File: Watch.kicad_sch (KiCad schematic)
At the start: 47 parts, among them J1 USB_C_Receptacle_USB2.0_14P, Q1 2N3904, Q2 2N3904, Q3 2N3904, Q4 2N3904, SW1 SW_Push, SW3 SW_Push, SW4 SW_Push, U1 MCP73831-2-OT, U2 KCSA02-105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

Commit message: session 2
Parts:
- removed C3: C, Capacitor_SMD:C_0603_1608Metric, symbol Device:C
- removed R13, R14, R15, R16: 150, Resistor_SMD:R_0603_1608Metric, symbol Device:R
- C2, C4: value C -> 4.7µF
- R10, R11, R12, R5: footprint Resistor_SMD:R_0603_1608Metric -> (none)
- renumbered U2 to Dig1, U4 to Dig2, U5 to Dig3, U6 to Dig4
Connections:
- net A: now also U7.5 (PA04); no longer R5.1
- net B: now also U7.6 (PA05); no longer R10.1
- net C: now also U7.7 (PA06); no longer R11.1
- net D: now also U7.8 (PA07); no longer R12.1
- net DIG1: now also R5.1; no longer Dig1.3 (CA), Dig1.8 (CA)
- net DIG2: now also R10.1; no longer Dig2.3 (CA), Dig2.8 (CA)
- net DIG3: now also R11.1; no longer Dig3.3 (CA), Dig3.8 (CA)
- net DIG4: now also R12.1; no longer Dig4.3 (CA), Dig4.8 (CA)
- net DP: now also U7.14 (PA11)
- net E: now also U7.11 (PA08)
- net F: now also U7.12 (PA09)
- net G: now also U7.13 (PA10)
- net at R5.2: now also Dig1.3 (CA), Dig1.8 (CA); no longer U7.5 (PA04)
- net at R10.2: now also Dig2.3 (CA), Dig2.8 (CA); no longer U7.6 (PA05)
- net at R11.2: now also Dig3.3 (CA), Dig3.8 (CA); no longer U7.7 (PA06)
- net at R12.2: now also Dig4.3 (CA), Dig4.8 (CA); no longer U7.8 (PA07)

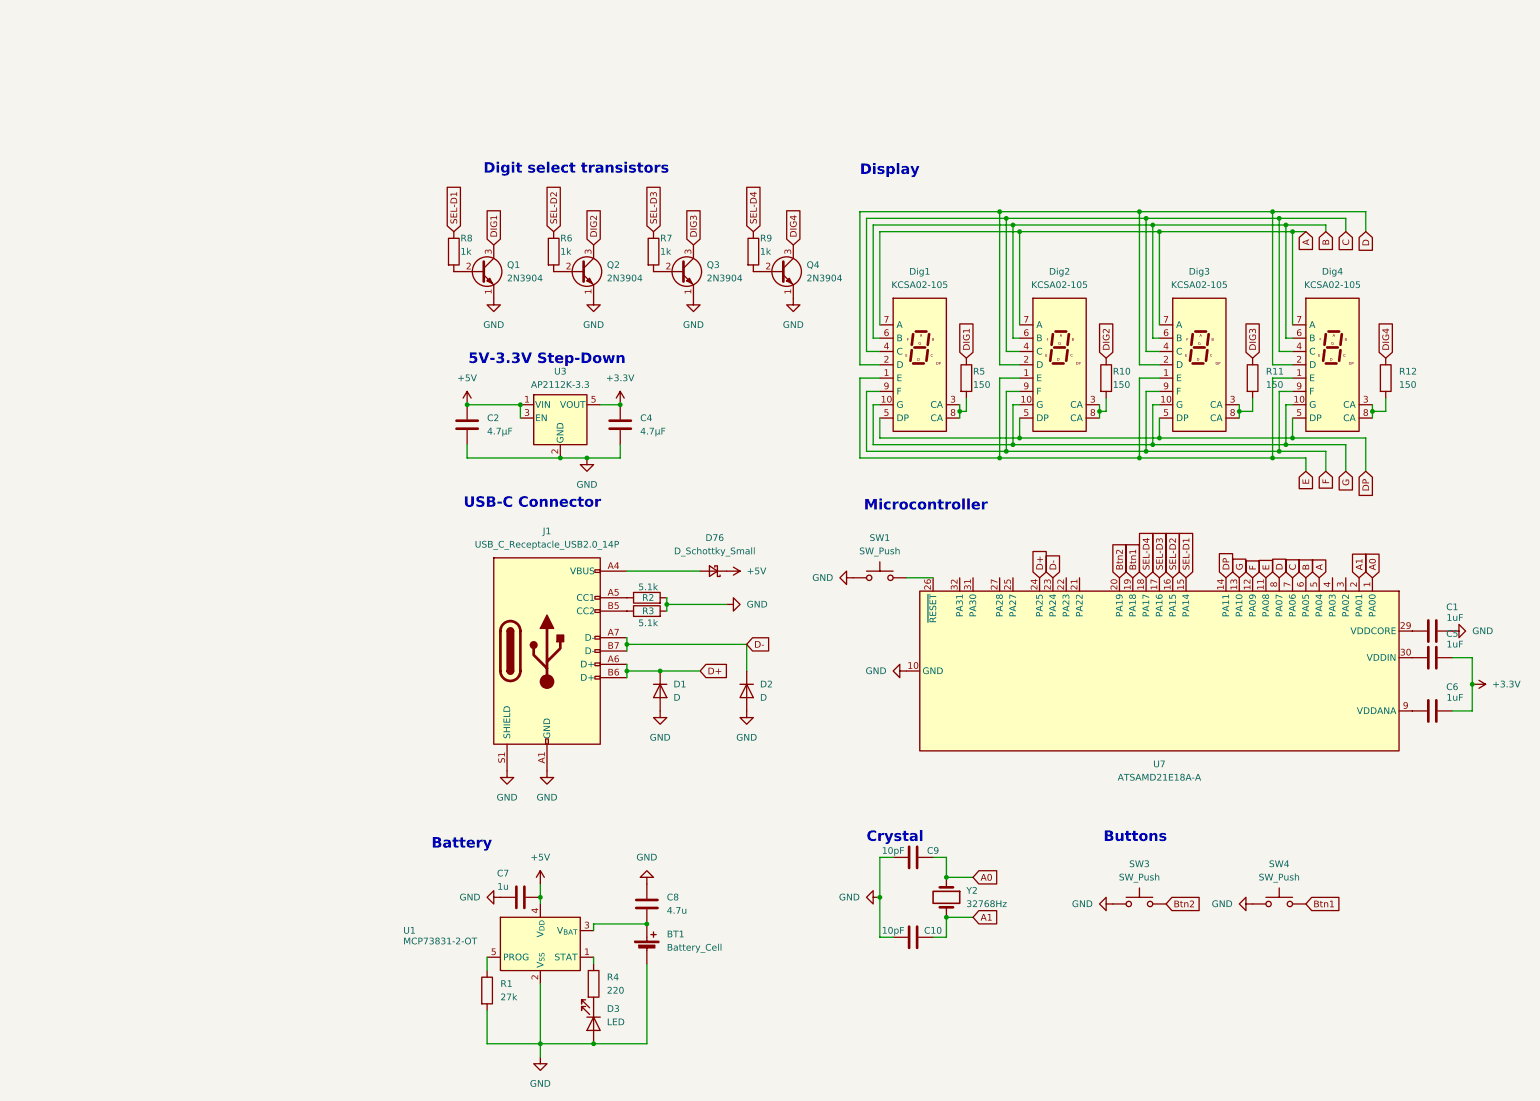
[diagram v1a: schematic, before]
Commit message: Add blender, session 4, new render
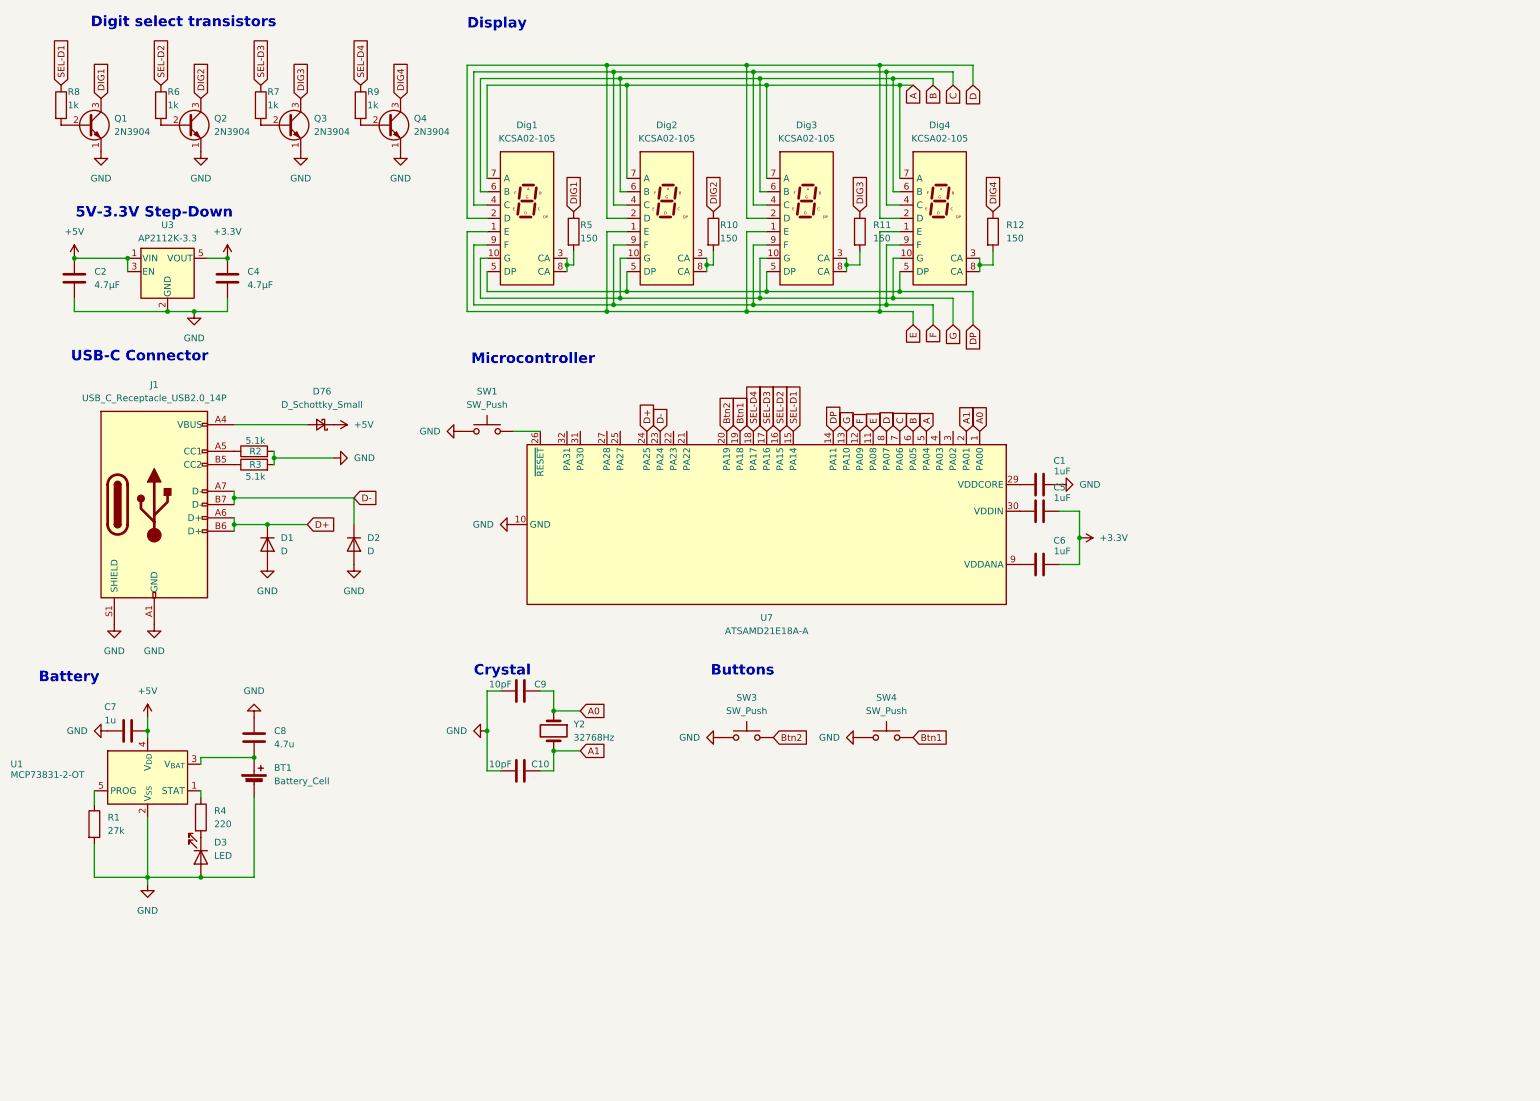
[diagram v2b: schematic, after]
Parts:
- D1, D2: footprint Diode_SMD:D_SOD-882D -> Diode_SMD:D_SOD-323
- D76: footprint Diode_SMD:D_0603_1608Metric -> Diode_SMD:D_SOD-323
- R1: footprint Resistor_SMD:R_0201_0603Metric -> Resistor_SMD:R_0603_1608Metric
- R10, R11, R12, R5: footprint (none) -> Resistor_SMD:R_0603_1608Metric
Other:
- moved on the sheet: BT1, C1, C10, C2, C4, C5, C6, C7, C8, C9, D1, D2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

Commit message: Fix PCB by adding test points
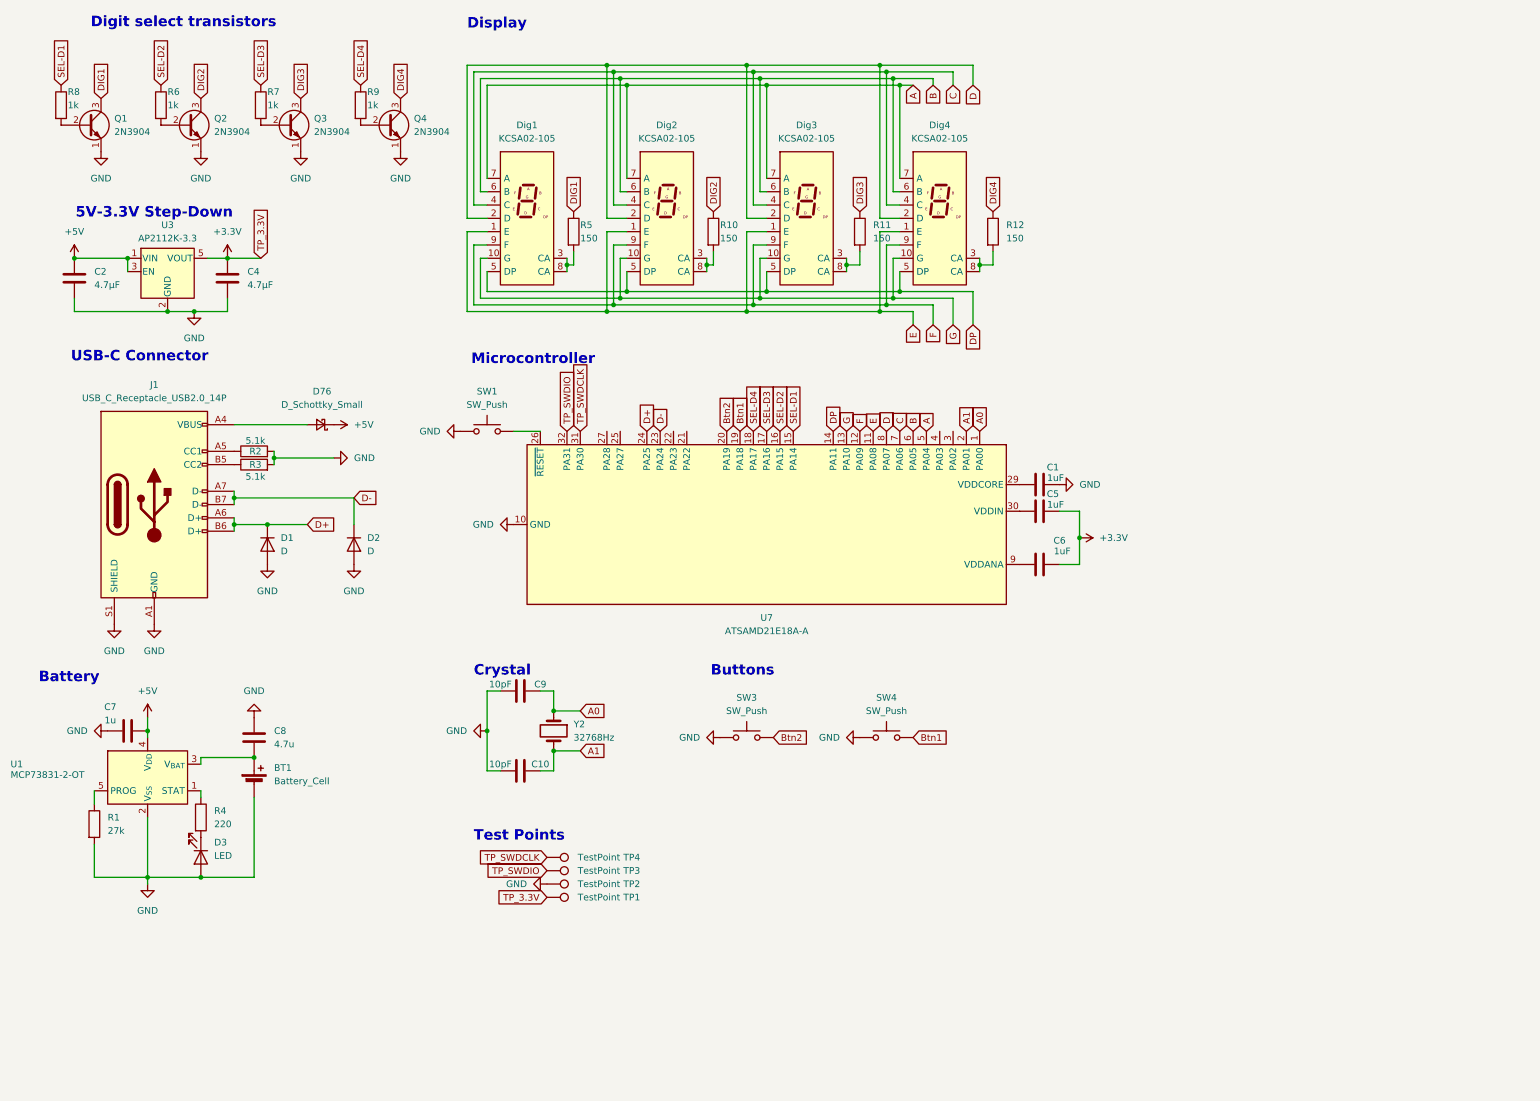
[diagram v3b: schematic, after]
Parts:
- added TP1, TP2, TP3, TP4: TestPoint, TestPoint:TestPoint_Pad_D1.0mm, symbol Connector:TestPoint
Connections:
- net +3.3V: now also TP1.1
- net GND: now also TP2.1
- net TP_SWDCLK: now reaches U7.31 (PA30)
- net TP_SWDCLK: now also TP4.1
- net TP_SWDIO: now reaches U7.32 (PA31)
- net TP_SWDIO: now also TP3.1
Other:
- note added: "Test Points"

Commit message: Better test points
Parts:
- added TP5: TestPoint, symbol Connector:TestPoint
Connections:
- new net TP_RST: TP5.1
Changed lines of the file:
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@@
+		)
+	)
+	(global_label "TP_RST"
+		(shape input)
+		(at 171.45 240.03 180)
+		(fields_autoplaced yes)
+		(effects
+			(font
+				(size 1.27 1.27)
+			)
+			(justify right)
+		)
+		(property "Intersheetrefs" "${INTERSHEET_REFS}"
+			(at 161.8125 240.03 0)
+			(effects
+				(font
+					(size 1.27 1.27)
+				)
+				(justify right)
+				(hide yes)
+			)
 		)
 	)
@@
 					(unit 1)
 				)
+			)
+		)
+	)
+	(symbol
+		(lib_id "Connector:TestPoint")
+		(at 171.45 240.03 270)
+		(unit 1)
+		(exclude_from_sim no)
+		(in_bom yes)
+		(on_board yes)
+		(dnp no)
+		(property "Reference" "TP5"
+			(at 185.674 240.03 90)
+			(effects
+				(font
+					(size 1.27 1.27)
+				)
+				(justify left)
+			)
+		)
+		(property "Value" "TestPoint"
+			(at 176.53 240.03 90)
+			(effects
+				(font
+					(size 1.27 1.27)
+				)
+				(justify left)
+			)
+		)
+		(property "Footprint" ""
+			(at 171.45 245.11 0)
+			(effects
+				(font
+					(size 1.27 1.27)
+				)
+				(hide yes)
+			)
+		)
+		(property "Datasheet" "~"
+			(at 171.45 245.11 0)
+			(effects
+				(font
+					(size 1.27 1.27)
+				)
+				(hide yes)
+			)
+		)
+		(property "Description" "test point"
+			(at 171.45 240.03 0)
+			(effects
+				(font
+					(size 1.27 1.27)
+				)
+				(hide yes)
+			)
+		)
+		(pin "1"
+		)
+		(instances
+			(project ""
+				(path "/e5022d08-9dda-4e3a-b81c-bab3a6fb67af"
+					(reference "TP5")
+					(unit 1)
+				)
